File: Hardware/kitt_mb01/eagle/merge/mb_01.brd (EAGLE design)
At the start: 160 x 100 mm, 124 parts, among them IC1.01 RT8293A, IC2.00 BQ24266RGET, IC3.01 LSM9DS1, U0.1 SI1922EDH, U6.01 TPS61032RSARPSDO-G16, U7.01 SI1922EDH, U7.2 SI1922EDH, X2.01 S2B-PH-K-S(LF)(SN), X7.02 ARDUINO_UNO, X7.03 CON_HEADER_1X02, X7.05 MOTOR, X7.06 CON_HEADER_1X02, X7.08 CON_HEADER_1X02, X7.09 0R-JUMPA, X7.10 0R-JUMPA, X7.11 CON_HEADER_1X02

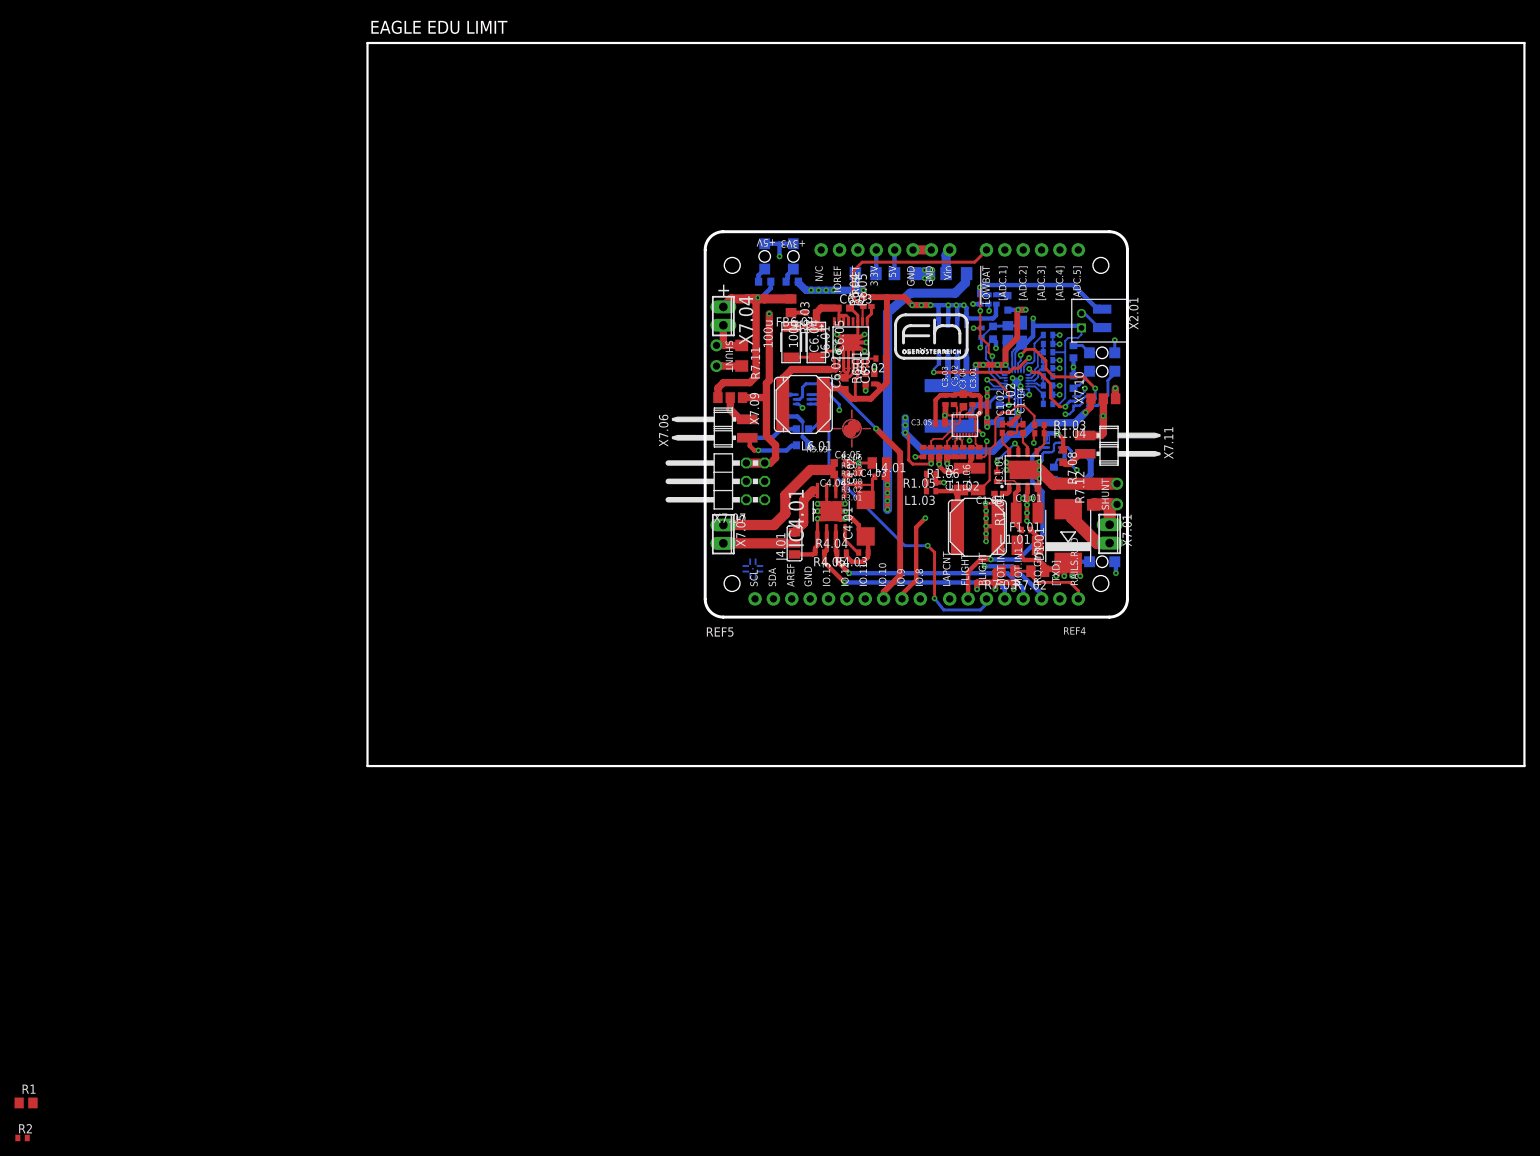
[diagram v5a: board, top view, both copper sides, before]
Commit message: changed yet more footprints -> mainly the beads, stepped it up to a beefier part,    can handle 6A, should be better than the previous 1A rating
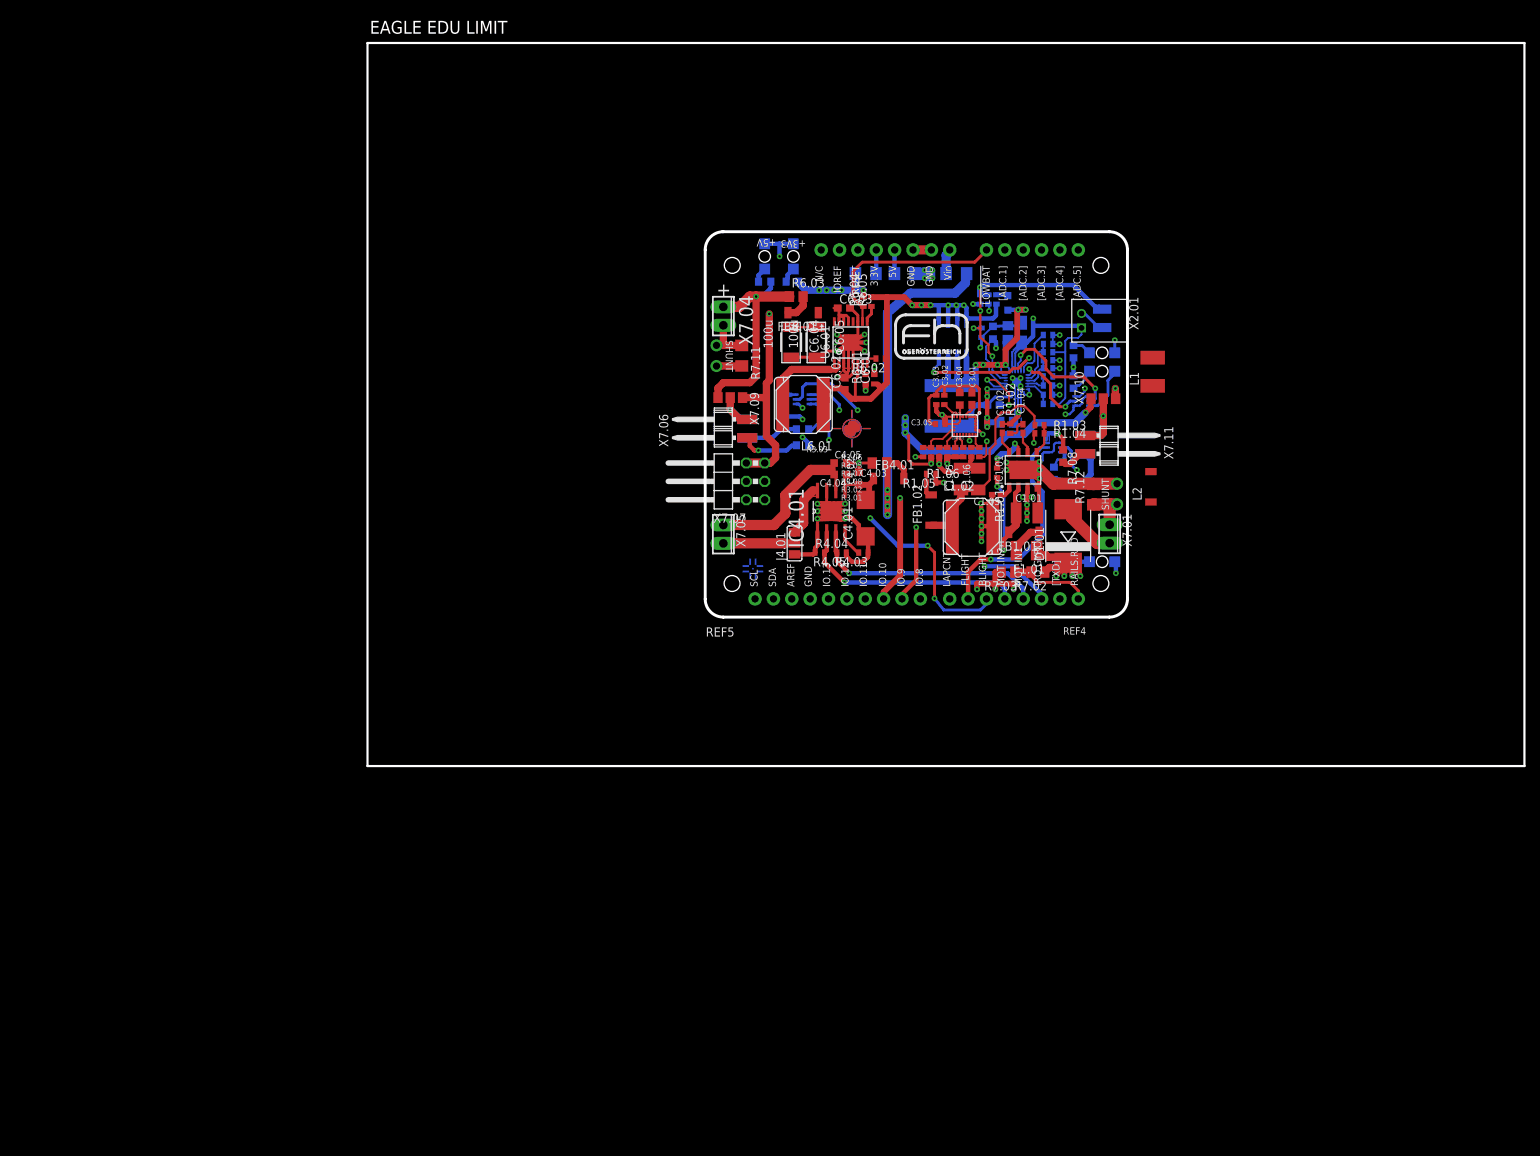
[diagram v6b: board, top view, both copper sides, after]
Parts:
- removed L1.01, L1.03, L4.01: BEAD, inductors:0402
- removed R1: (no value), rcl:R0805
- removed R2: (no value), rcl:R0402
- added FB1.01, FB1.02, FB4.01: BEAD, rcl:L4516C
- added L1: (no value), rcl:L1812
- added L2: (no value), rcl:L4516C
- C3.01: device rcl:C0402 -> rcl:C0603
- FB6.01: device inductors:0402 -> rcl:L4516C
- moved R6.03 1.46 mm to (59.3, 64.9), turned to 0 degrees
- moved C3.02 1.35 mm to (79.8, 50.6)
- moved C3.03 1.27 mm to (78.7, 50.6)
- moved FB6.01 1.03 mm to (60.2, 62.7)
- moved F1.01 0.75 mm to (91.1, 29.8), turned to 180 degrees
- moved L1.02 0.71 mm to (83.4, 33.0)
- moved R1.01 0.56 mm to (87.1, 40.6)
- moved C3.04 0.54 mm to (81.9, 50.8)
- moved C1.03 0.35 mm to (87.0, 37.5)
- moved C3.01 0.18 mm to (83.6, 50.8)
- moved R7.03 0.16 mm to (88.6, 26.8)
- moved R7.02 0.12 mm to (92.7, 26.8)
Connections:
- net +12V: now also FB4.01.2; no longer L4.01.2
- net N$10: now also FB4.01.1; no longer L4.01.1
- net N$80: now also FB1.01.1; no longer L1.01.1
- net N$81: now also FB1.01.2; no longer L1.01.2
- net N$87: now also FB1.02.1; no longer L1.03.1
- net N$90: now also FB1.02.2; no longer L1.03.2
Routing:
- net N$81: track 10.9 -> 20.9 mm, vias 0 -> 2
- net GND: track 239.7 -> 245.9 mm
- net N$43: track 13.9 -> 9.09 mm
- net +12V: track 104.7 -> 107.6 mm
- net !IRQ_GYRO: track 37.4 -> 39.8 mm
- net N$80: track 2.49 -> 4.52 mm
- net N$36: track 2.05 -> 3.77 mm
- net N$88: track 16.5 -> 18.0 mm
- net +3V3: track 160.5 -> 161.7 mm
- net N$90: track 2.38 -> 3.38 mm
- net CAR.AUXILLARY: track 41.2 -> 40.2 mm, vias 1 -> 2
- net N$6: track 1.85 -> 2.76 mm
- net N$10: track 10.2 -> 9.40 mm
- net CAR.GATECTLR: track 40.2 -> 40.7 mm
- net CAR.BLIGHT: track 46.7 -> 46.3 mm, vias 2 -> 4
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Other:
- board text removed: "CHANGE LED RES TO 0805"

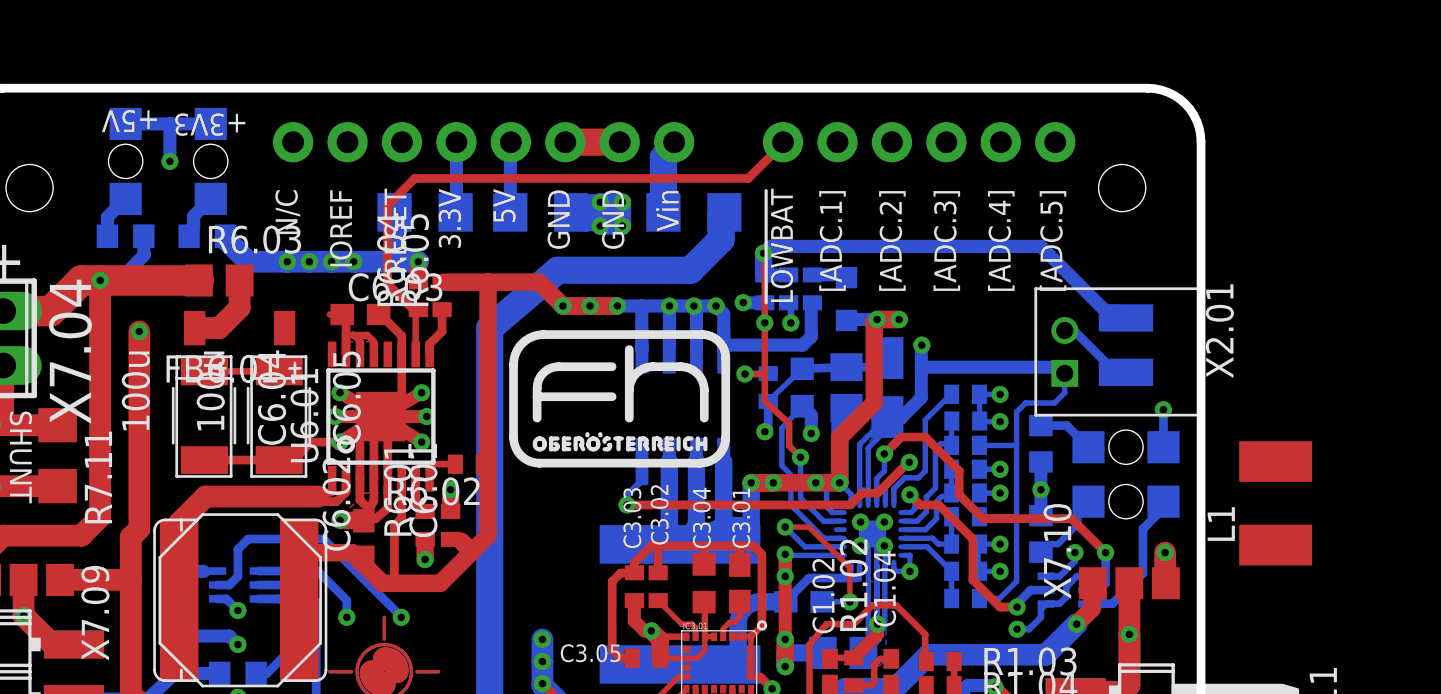
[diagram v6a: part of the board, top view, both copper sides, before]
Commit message: updated BOM and board, components have all been selected for this board
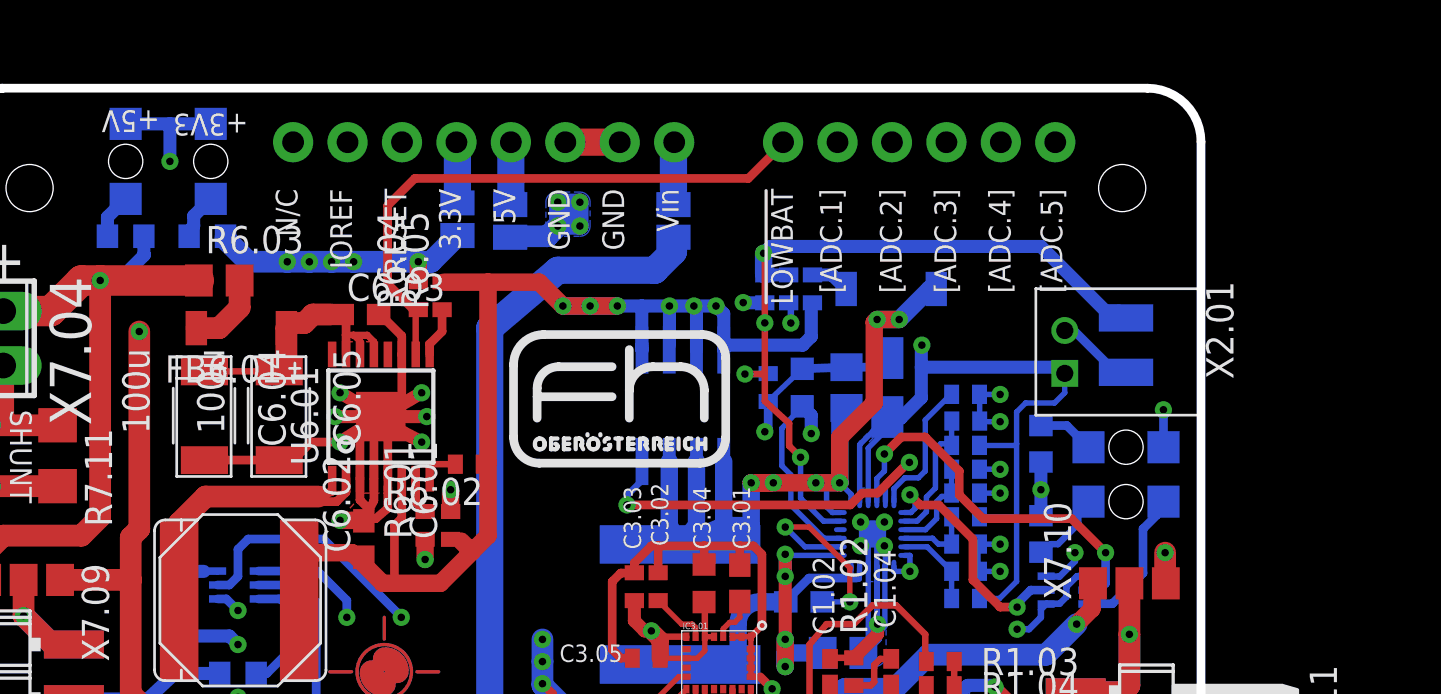
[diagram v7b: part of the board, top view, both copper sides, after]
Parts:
- removed L1: (no value), rcl:L1812
- removed L2.02: BEAD, rcl:L2012C
- added FB2.01: BEAD, rcl:L4516C
- C1.04: value XX -> 3.3nF
- C4.03: value (none) -> 4.7uF
- L1.02: value 4.7uH -> 15uH
- R1.02: value XX -> 20kR
- R1.03: value XX -> 62kR
- R1.04: value XX -> 11.8kR
- R7.05, R7.06, R7.07: device rcl:R1206 -> jumper:SJ
- moved R7.05 1.54 mm to (70.4, 67.8), turned to 90 degrees
- moved R7.06 1.48 mm to (72.9, 67.7), turned to 90 degrees
- moved R7.07 1.03 mm to (80.5, 67.7), turned to 90 degrees
- moved FB6.01 0.08 mm to (60.3, 62.7)
- renumbered U0.1 to U7.03
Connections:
- net N$16: now also FB2.01.2; no longer L2.02.2
- net N$18: now also FB2.01.1; no longer L2.02.1
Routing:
- net N$43: track 9.09 -> 13.7 mm
- net +12V: track 107.6 -> 104.5 mm
- net +5V: track 154.0 -> 151.0 mm
- net N$18: track 42.9 -> 43.8 mm
- net N$5: track 3.48 -> 2.88 mm
- added copper zone on layer 16, net +5V
